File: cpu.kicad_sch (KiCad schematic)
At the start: 13 parts, among them J21 KEYBOARD IRQ, J22 BUS IRQ, J23 VIDEO IRQ, K17 CPU_CLK, P37 CPU OSC, U14 74LS125, U2 74LS14, U33 74LS10, U52 Z8S180, U7 74LS32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

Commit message: rev 1.0
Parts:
- removed U8: 74LS08, Custom:STD_DDW_DIP14, symbol 74xx:74LS08
- added P19: ASCI OSC, Custom:STD_DDW_DIP14, symbol Custom:CLK
- added R12, R8: 4700, Custom:STD_DDW_RESISTOR, symbol Device:R
- added U34: 74LS393, Custom:STD_DDW_DIP14, symbol 74xx:74LS393
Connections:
- net DATA_DIR: now also U7.11
- net GND: now also P19.4, P19.5, P19.6, P19.7, U34.12 (MR)
- net VCC: now also P19.14
- net /BUSAK: no longer U33.5
- net /DREQ0: now also R8.1
- net /M1: no longer U33.4
- net /MREQ: now also U33.4
- net /RD: no longer U33.3
- net /TEND0: now also R12.1
- net at U33.6: now also U7.13
- new net: R12.2, R8.2, U34.8 (Q3)
- new net: P19.10, P19.11, P19.8, P19.9, U34.13 (CP)
- new net /CS_RTC: U33.3
- new net /INTIORQ: U33.5
- no-connect marks 15 -> 21
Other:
- moved on the sheet: U33B

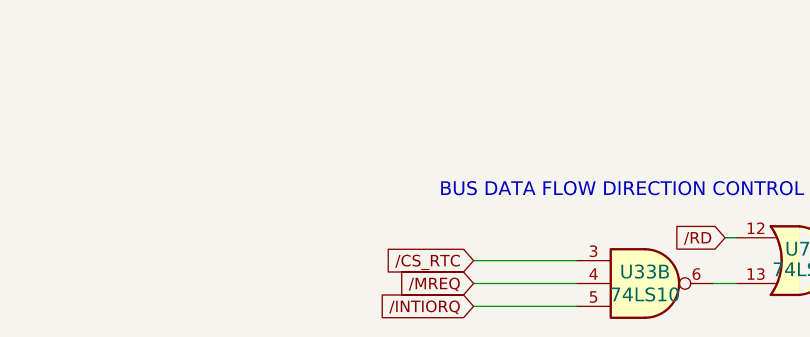
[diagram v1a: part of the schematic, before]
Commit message: V1.1 PCB and schematic fix issue with data direction for bus
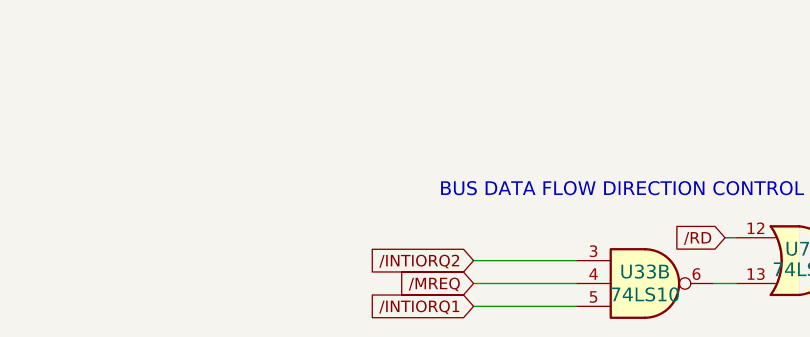
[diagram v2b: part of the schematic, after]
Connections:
- net /CS_RTC renamed /INTIORQ2
- net /INTIORQ renamed /INTIORQ1
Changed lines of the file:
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@@
 	(title_block
 		(title "N8PC")
-		(date "2025-11-26")
-		(rev "000.9")
+		(date "2025-12-13")
+		(rev "001.1")
 		(comment 1 "https://github.com/danwerner21/N8PC")
 		(comment 2 "Based on work by Andrew Lynch and John Coffman")
@@
 		)
 	)
-	(global_label "{slash}CS_RTC"
+	(global_label "{slash}INTIORQ1"
 		(shape input)
-		(at 177.8 194.31 180)
+		(at 177.8 199.39 180)
 		(fields_autoplaced yes)
 		(effects
@@
 		)
 		(property "Intersheetrefs" "${INTERSHEET_REFS}"
-			(at 167.1838 194.31 0)
+			(at 165.4903 199.39 0)
 			(effects
 				(font
@@
 		)
 	)
+	(global_label "{slash}INTIORQ2"
+		(shape input)
+		(at 177.8 194.31 180)
+		(fields_autoplaced yes)
+		(effects
+			(font
+				(size 1.27 1.27)
+			)
+			(justify right)
+		)
+		(property "Intersheetrefs" "${INTERSHEET_REFS}"
+			(at 165.4903 194.31 0)
+			(effects
+				(font
+					(size 1.27 1.27)
+				)
+				(justify right)
+				(hide yes)
+			)
+		)
+	)
 	(global_label "A17"
 		(shape output)
@@
 				(hide yes)
 			)
-		)
-	)
-	(global_label "{slash}INTIORQ"
-		(shape input)
-		(at 177.8 199.39 180)
-		(fields_autoplaced yes)
-		(effects
-			(font
-				(size 1.27 1.27)
-			)
-			(justify right)
-		)
-		(property "Intersheetrefs" "${INTERSHEET_REFS}"
-			(at 166.6998 199.39 0)
-			(effects
-				(font
-					(size 1.27 1.27)
-				)
-				(justify right)
-				(hide yes)
-			)
